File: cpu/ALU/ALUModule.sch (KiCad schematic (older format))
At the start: 70 parts

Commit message: Completed initial version of ALU. Created blank memory schematic.
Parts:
- added C1, C10, C11, C12, C13, C14, C15, C16, C17, C18, C19, C2, C20, C21, C22, C23, C24, C25, C26, C27, C28, C29, C3, C30, C31, C32, C33, C34, C35, C36, C37, C38, C39, C4, C40, C41, C42, C43, C5, C6, C7, C8, C9: 0.1uF, symbol Device:C
- added U10, U11, U12, U13, U14, U15, U16, U17, U18, U24, U25, U26, U27, U28, U29, U3, U30, U31, U32, U4, U44, U5, U6, U7, U8, U9: 74LS253, symbol 74xx:74LS253
- added U21, U33: 74LS02, symbol 74xx:74LS02
- added U22, U23: 74LS08, symbol 74xx:74LS08
- added U34: 74LS86, symbol 74xx:74LS86
- added U35, U36, U37, U38: 74LS283, symbol 74xx:74LS283
- added U39, U40, U41, U42, U43: 74LS574, symbol 74xx:74LS574
- U1, U19, U2, U20: renamed from U?; symbol 74ls245_bidirection:74LS245_BiDirection -> ALUModule-rescue:74LS245_BiDirection-74ls245_bidirection
- gave numbers to parts that had none: 66
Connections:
- net labels added: add_00, add_01, add_02, add_03, add_04, add_05, add_06, add_07, add_08, add_09, add_10, add_11, add_12, add_13, add_14, add_15, arr_carry_in, arr_carry_out, arr_carry_select_0, arr_carry_select_1, arrithmetic_carry_flag, bit_control_0, bit_control_1, bit_control_2, bit_control_3, lgc_carry_held, logical_00, logical_01, logical_02, logical_03, logical_04, logical_05, logical_06, logical_07, logical_08, logical_09, logical_10, logical_11, logical_12, logical_13, logical_14, logical_15, logical_carry_flag, overflow_flag, shift_00, shift_01, shift_02, shift_03, shift_04, shift_05, shift_06, shift_07, shift_08, shift_09, shift_10, shift_11, shift_12, shift_13, shift_14, shift_15, shift_control_0, shift_control_1, sign_flag, x_latched_00, x_latched_01, x_latched_02, x_latched_03, x_latched_04, x_latched_05, x_latched_06, x_latched_07, x_latched_08, x_latched_09, x_latched_10, x_latched_11, x_latched_12, x_latched_13, x_latched_14, x_latched_15, y_latched_00, y_latched_01, y_latched_02, y_latched_03, y_latched_04, y_latched_05, y_latched_06, y_latched_07, y_latched_08, y_latched_09, y_latched_10, y_latched_11, y_latched_12, y_latched_13, y_latched_14, y_latched_15, zero_flag
- net labels removed: HLT, RST, ~CLK
- wire segments 238 -> 1251
- no-connect marks 0 -> 121
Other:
- note added: "Adder"
- note added: "Bitwise Operations"
- note added: "Bitwise operations support the\nfollowing operations. The control\ninput values are give for each\noperation.\n\n[0000] ZERO\n[0011] NOT y\n[0110] x XOR y\n[1000] x AND y\n[1100] Y\n[1110] x OR y\n[1111] 255\n\nNOTE: We are only using one\nof two available selectors in\neach chip. It is possible to swap\nwhich one is used to make\nrouting easier.\n\nNOTE: There are more combinations\nof control i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"
- note added: "Bus Displays"
- note added: "Flags"
- note added: "Flags logic. After an operation the flag\nlines are updated\n\nThe following flags are supported\n0: Zero: did the operation result in a zero\n value\n1: Logical Carry: did a logical operation\n result in a carry\n2: Arrithmetic Carry: did an arithetic\n operation result in a carry\n3: Sign: did the operation result in a negative\n value (high bit on)\n4: Overflow: did the operation result in an\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"
- note added: "Intermediate Latches"
- note added: "Shift Operations"
- note added: "Shifter supports passthrough,\nshift-left, shift-right and zero.\nThe 'shift_control_X' lines control\nwhich functionality to use.\n\n[00]: Unchanged\n[01]: Shift Left\n[10]: Shift Right\n[11]: Zero"
- note added: "X Bus"
- note added: "Y Bus"
- moved on the sheet: D1, D10, D11, D12, D13, D14, D15, D16, D17, D18, D19, D2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

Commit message: ALU and constant register first version
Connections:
- wire segments 1251 -> 1249
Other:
- moved on the sheet: C1, C10, C11, C12, C13, C14, C15, C16, C17, C18, C19, C2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

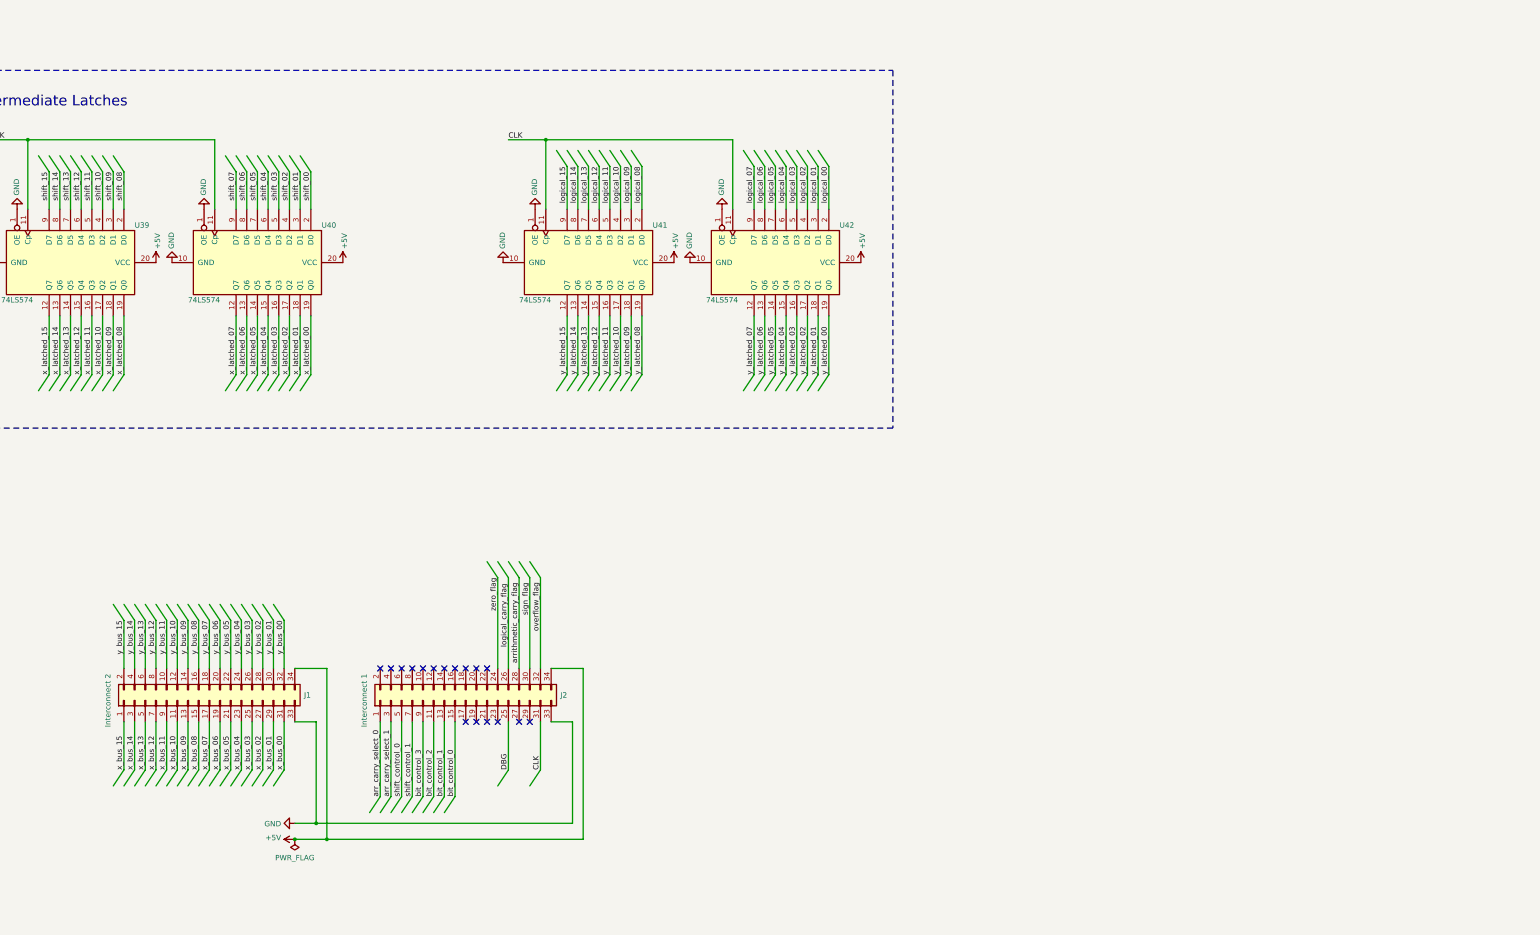
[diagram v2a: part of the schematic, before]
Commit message: Update ALU schematic with D_BUS connection, added test points.
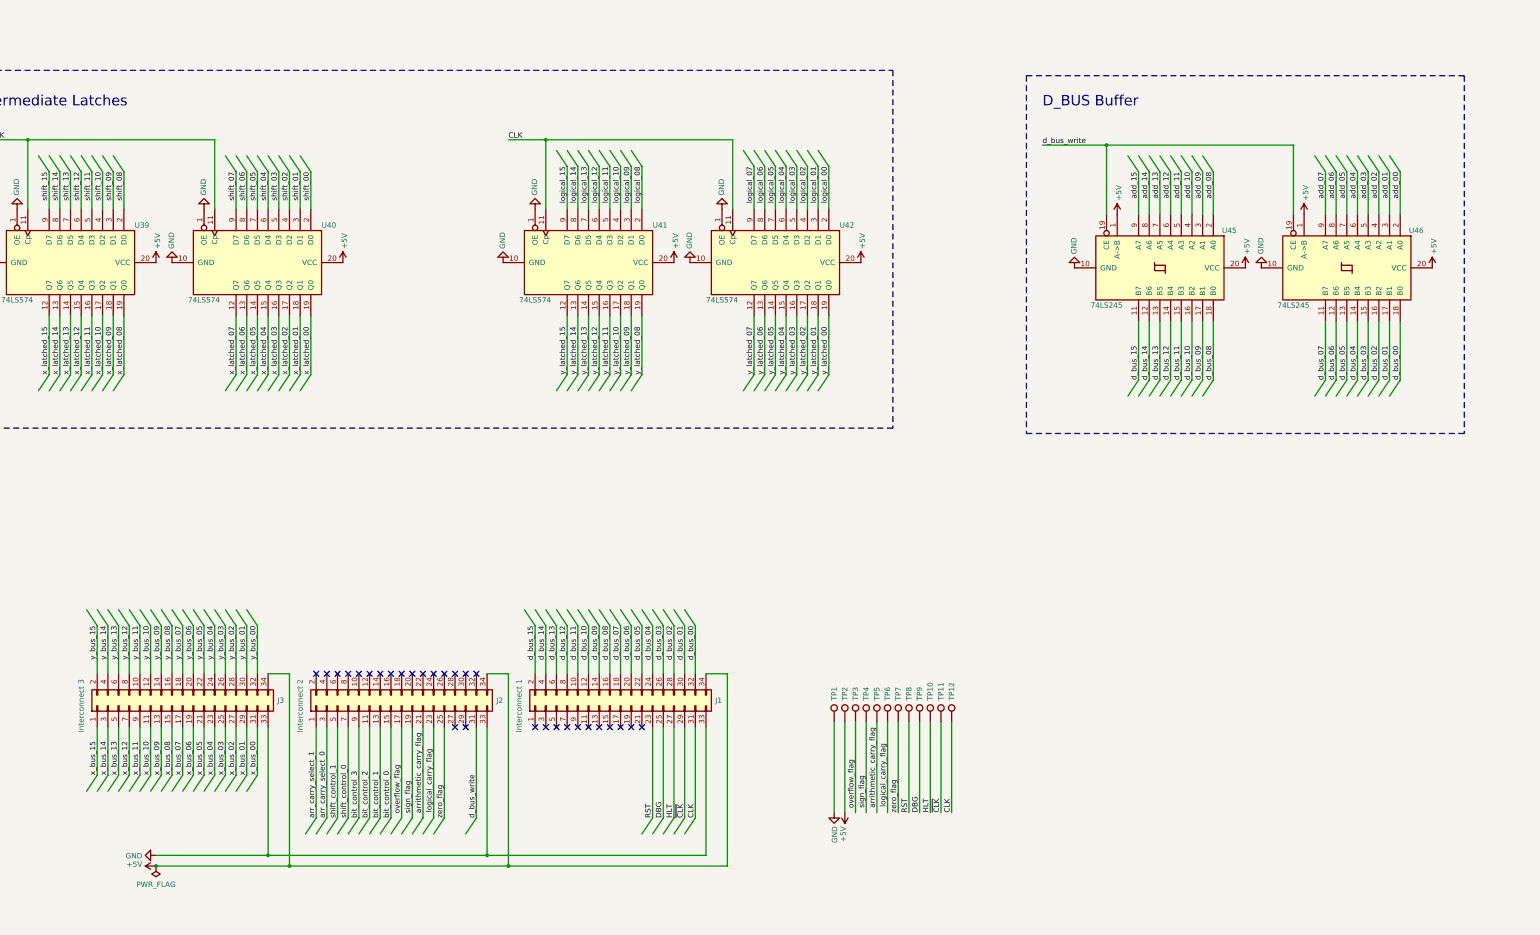
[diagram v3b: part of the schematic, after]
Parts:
- added J2: Interconnect 2, symbol Connector_Generic:Conn_02x17_Odd_Even
- added TP1, TP10, TP11, TP12, TP2, TP3, TP4, TP5, TP6, TP7, TP8, TP9: TestPoint, TestPoint:TestPoint_Pad_D1.5mm, symbol Connector:TestPoint
- added U45, U46: 74LS245, symbol ALUModule-rescue:74LS245_BiDirection-74ls245_bidirection
- J3: renamed from J1; value Interconnect 2 -> Interconnect 3
- renumbered J2 to J1
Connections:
- net labels added: HLT, RST, d_bus_00, d_bus_01, d_bus_02, d_bus_03, d_bus_04, d_bus_05, d_bus_06, d_bus_07, d_bus_08, d_bus_09, d_bus_10, d_bus_11, d_bus_12, d_bus_13, d_bus_14, d_bus_15, d_bus_write, ~CLK
- wire segments 1249 -> 1372
- no-connect marks 121 -> 133
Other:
- note added: "D_BUS Buffer"
- moved on the sheet: J1, J3

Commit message: Working on ALU PCB
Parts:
- C1, C10, C11, C12, C13, C14, C15, C16, C17, C18, C19, C2, C20, C21, C22, C23, C24, C25, C26, C27, C28, C29, C3, C30, C31, C32, C33, C34, C35, C36, C37, C38, C39, C4, C40, C41, C42, C43, C5, C6, C7, C8, C9: footprint (none) -> Capacitor_SMD:C_0603_1608Metric_Pad1.05x0.95mm_HandSolder
- D1, D10, D11, D12, D13, D14, D15, D16, D17, D18, D19, D2, D20, D21, D22, D23, D24, D25, D26, D27, D28, D29, D3, D30, D31, D32, D4, D5, D6, D7, D8, D9: footprint (none) -> LED_SMD:LED_1206_3216Metric_Pad1.42x1.75mm_HandSolder
- J1, J2, J3: footprint (none) -> Connector_PinHeader_2.54mm:PinHeader_2x17_P2.54mm_Horizontal
- R1, R10, R11, R12, R13, R14, R15, R16, R17, R18, R19, R2, R20, R21, R22, R23, R24, R25, R26, R27, R28, R29, R3, R30, R31, R32, R4, R5, R6, R7, R8, R9: footprint (none) -> Resistor_SMD:R_0603_1608Metric_Pad1.05x0.95mm_HandSolder
- U1, U19, U2, U20, U39, U40, U41, U42, U43, U45, U46: footprint (none) -> Package_SO:SOIC-20W_7.5x12.8mm_P1.27mm
- U10, U11, U12, U13, U14, U15, U16, U17, U18, U24, U25, U26, U27, U28, U29, U3, U30, U31, U32, U35, U36, U37, U38, U4, U44, U5, U6, U7, U8, U9: footprint (none) -> Package_SO:SOIC-16_3.9x9.9mm_P1.27mm
- U21, U22, U23, U33, U34: footprint (none) -> Package_SO:SOIC-14_3.9x8.7mm_P1.27mm

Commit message: Finished a draft of the ALU PCB
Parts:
- removed J1: Interconnect 1, Connector_PinHeader_2.54mm:PinHeader_2x17_P2.54mm_Horizontal, symbol Connector_Generic:Conn_02x17_Odd_Even
- removed J2: Interconnect 2, Connector_PinHeader_2.54mm:PinHeader_2x17_P2.54mm_Horizontal, symbol Connector_Generic:Conn_02x17_Odd_Even
- removed J3: Interconnect 3, Connector_PinHeader_2.54mm:PinHeader_2x17_P2.54mm_Horizontal, symbol Connector_Generic:Conn_02x17_Odd_Even
- added C44, C45, C46, C47: 0.1uF, Capacitor_SMD:C_0603_1608Metric_Pad1.05x0.95mm_HandSolder, symbol Device:C
- added D33: overflow, LED_SMD:LED_1206_3216Metric_Pad1.42x1.75mm_HandSolder, symbol Device:LED_ALT
- added D34: sign, LED_SMD:LED_1206_3216Metric_Pad1.42x1.75mm_HandSolder, symbol Device:LED_ALT
- added D35: arithmetic_carry, LED_SMD:LED_1206_3216Metric_Pad1.42x1.75mm_HandSolder, symbol Device:LED_ALT
- added D36: logical_carry, LED_SMD:LED_1206_3216Metric_Pad1.42x1.75mm_HandSolder, symbol Device:LED_ALT
- added D37: zero, LED_SMD:LED_1206_3216Metric_Pad1.42x1.75mm_HandSolder, symbol Device:LED_ALT
- added J1: Bus_PCI_32bit_5V, Connector_PCBEdge:BUS_PCI, symbol cpu_custom_symbols:Bus_PCI_32bit_5V
- added R33, R34, R35, R36, R37: 220R, Resistor_SMD:R_0603_1608Metric_Pad1.05x0.95mm_HandSolder, symbol Device:R
- added U47: 74LS245, Package_SO:SOIC-20W_7.5x12.8mm_P1.27mm, symbol ALUModule-rescue:74LS245_BiDirection-74ls245_bidirection
- TP1: value TestPoint -> GND
- TP10: value TestPoint -> HLT
- TP11: value TestPoint -> ~CLK
- TP12: value TestPoint -> CLK
- TP2: value TestPoint -> +5
- TP3: value TestPoint -> FLG Overflow
- TP4: value TestPoint -> FLG Sign
- TP5: value TestPoint -> FLG ArithCarry
- TP6: value TestPoint -> FLG LogCarry
- TP7: value TestPoint -> FLG Zero
- TP8: value TestPoint -> RST
- TP9: value TestPoint -> DBG
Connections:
- net labels added: arithmetic_carry_flag
- wire segments 1372 -> 1414
- no-connect marks 133 -> 155
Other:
- moved on the sheet: D1, D10, D11, D12, D13, D14, D15, D16, D17, D18, D19, D2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

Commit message: Completed GPR 1.2 PCB and started lots of other things. * Started ALU * Updated Constant Reg * Completed v1.2 GPR * Added random symbols * Updated Memory * Updated plots
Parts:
- J1: symbol cpu_custom_symbols:Bus_PCI_32bit_5V -> ALUModule-rescue:Bus_PCI_32bit_5V-cpu_custom_symbols
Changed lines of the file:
@@
 NoConn ~ 2950 19900
 $Comp
-L cpu_custom_symbols:Bus_PCI_32bit_5V J1
+L ALUModule-rescue:Bus_PCI_32bit_5V-cpu_custom_symbols J1
 U 1 1 699FC8B3
 P 5250 19000
